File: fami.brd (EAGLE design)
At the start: 86.4 x 50.8 mm, 14 parts, among them IC1 PROM, IC2 WRAM, IC3 CHROM, IC4 74LS20N

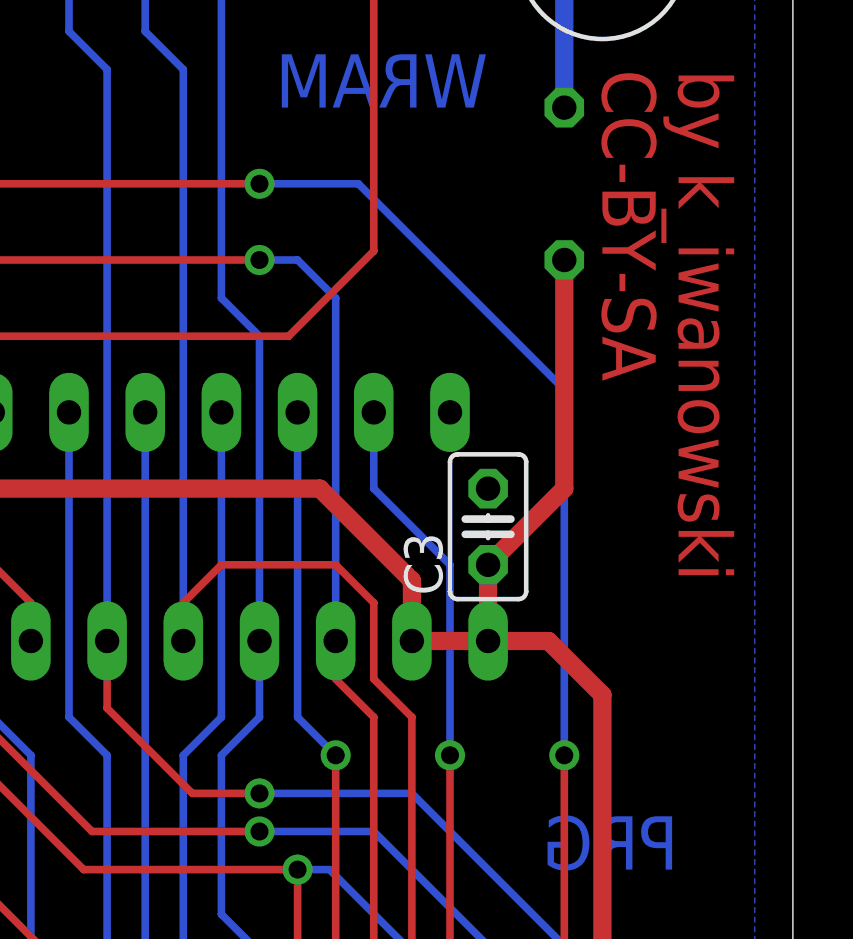
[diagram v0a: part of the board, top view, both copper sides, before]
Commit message: Added R and C values
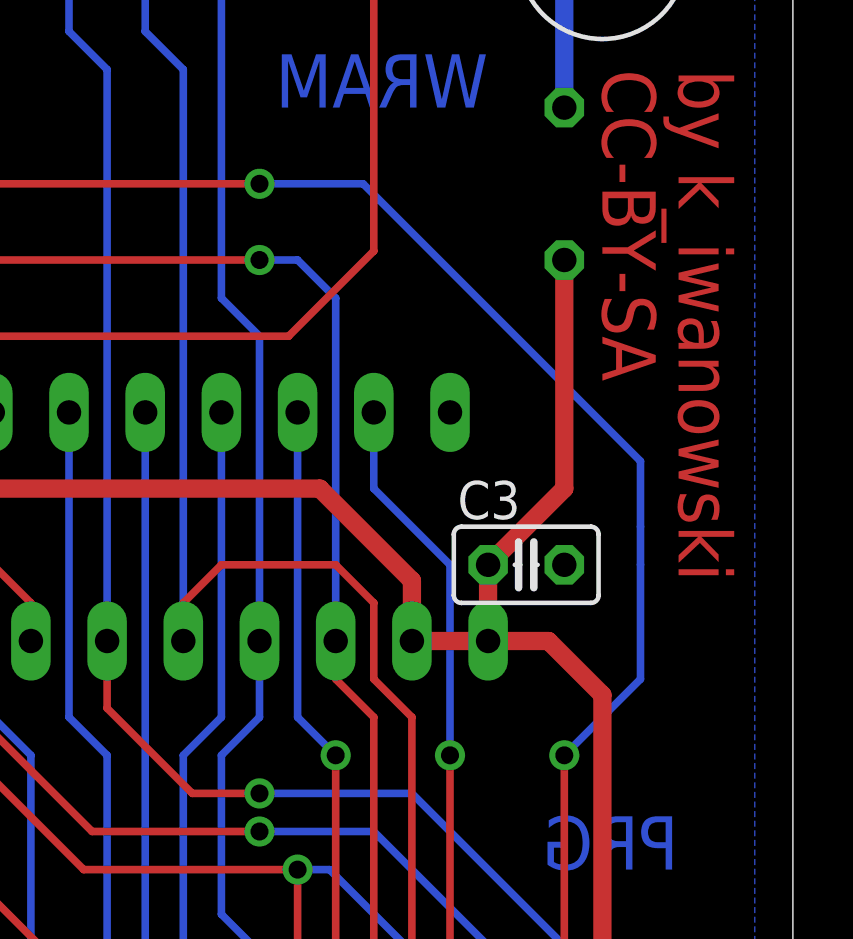
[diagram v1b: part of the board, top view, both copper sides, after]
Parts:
- C1: value (none) -> 10u
- C2, C3: value (none) -> 100n
- R1, R2: value (none) -> 1k
- moved C3 1.80 mm to (76.2, 22.9), turned to 0 degrees
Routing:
- net O2: track 88.9 -> 91.1 mm
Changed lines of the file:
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@@
 <element name="D2" library="diode" package="D-5" value="" x="35.56" y="48.26" rot="MR0"/>
 <element name="JP1" library="SparkFun-Connectors" package="1X03" value="" x="26.67" y="25.4" rot="MR0"/>
-<element name="C1" library="rcl" package="E2,5-6" value="" x="78.74" y="43.18"/>
-<element name="C2" library="rcl" package="C025-025X050" value="" x="33.02" y="25.4" rot="R180"/>
-<element name="R1" library="rcl" package="0204/7" value="" x="44.45" y="48.26" rot="R180"/>
-<element name="R2" library="rcl" package="0204/7" value="" x="44.45" y="45.72"/>
-<element name="C3" library="rcl" package="C025-025X050" value="" x="74.93" y="24.13" rot="R90"/>
+<element name="C1" library="rcl" package="E2,5-6" value="10u" x="78.74" y="43.18"/>
+<element name="C2" library="rcl" package="C025-025X050" value="100n" x="33.02" y="25.4" rot="R180"/>
+<element name="R1" library="rcl" package="0204/7" value="1k" x="44.45" y="48.26" rot="R180"/>
+<element name="R2" library="rcl" package="0204/7" value="1k" x="44.45" y="45.72"/>
+<element name="C3" library="rcl" package="C025-025X050" value="100n" x="76.2" y="22.86"/>
 <element name="G2" library="battery" package="B2430UNI" value="B2430UNI" x="11.43" y="38.1" rot="R180"/>
 </elements>
@@
 <wire x1="77.47" y1="2.54" x2="77.47" y2="16.51" width="0.254" layer="1"/>
 <via x="77.47" y="16.51" extent="1-16" drill="0.6"/>
-<wire x1="77.47" y1="16.51" x2="77.47" y2="28.698034375" width="0.254" layer="16"/>
-<wire x1="77.47" y1="28.698034375" x2="70.608034375" y2="35.56" width="0.254" layer="16"/>
-<wire x1="70.608034375" y1="35.56" x2="67.31" y2="35.56" width="0.254" layer="16"/>
+<wire x1="77.47" y1="16.51" x2="80.01" y2="19.05" width="0.254" layer="16"/>
+<wire x1="80.01" y1="19.05" x2="80.01" y2="22.86" width="0.254" layer="16"/>
+<wire x1="80.01" y1="22.86" x2="80.01" y2="24.13" width="0.254" layer="16"/>
 <via x="67.31" y="35.56" extent="1-16" drill="0.6"/>
 <wire x1="67.31" y1="35.56" x2="33.76395" y2="35.56" width="0.254" layer="1"/>
 <wire x1="33.76395" y1="35.56" x2="29.95395" y2="39.37" width="0.254" layer="1"/>
 <wire x1="29.95395" y1="39.37" x2="27.94" y2="39.37" width="0.254" layer="1"/>
+<wire x1="67.31" y1="35.56" x2="70.7642625" y2="35.56" width="0.254" layer="16"/>
+<wire x1="70.7642625" y1="35.56" x2="80.01" y2="26.3142625" width="0.254" layer="16"/>
+<wire x1="80.01" y1="26.3142625" x2="80.01" y2="24.13" width="0.254" layer="16"/>
 </signal>
 <signal name="VRAMA10">

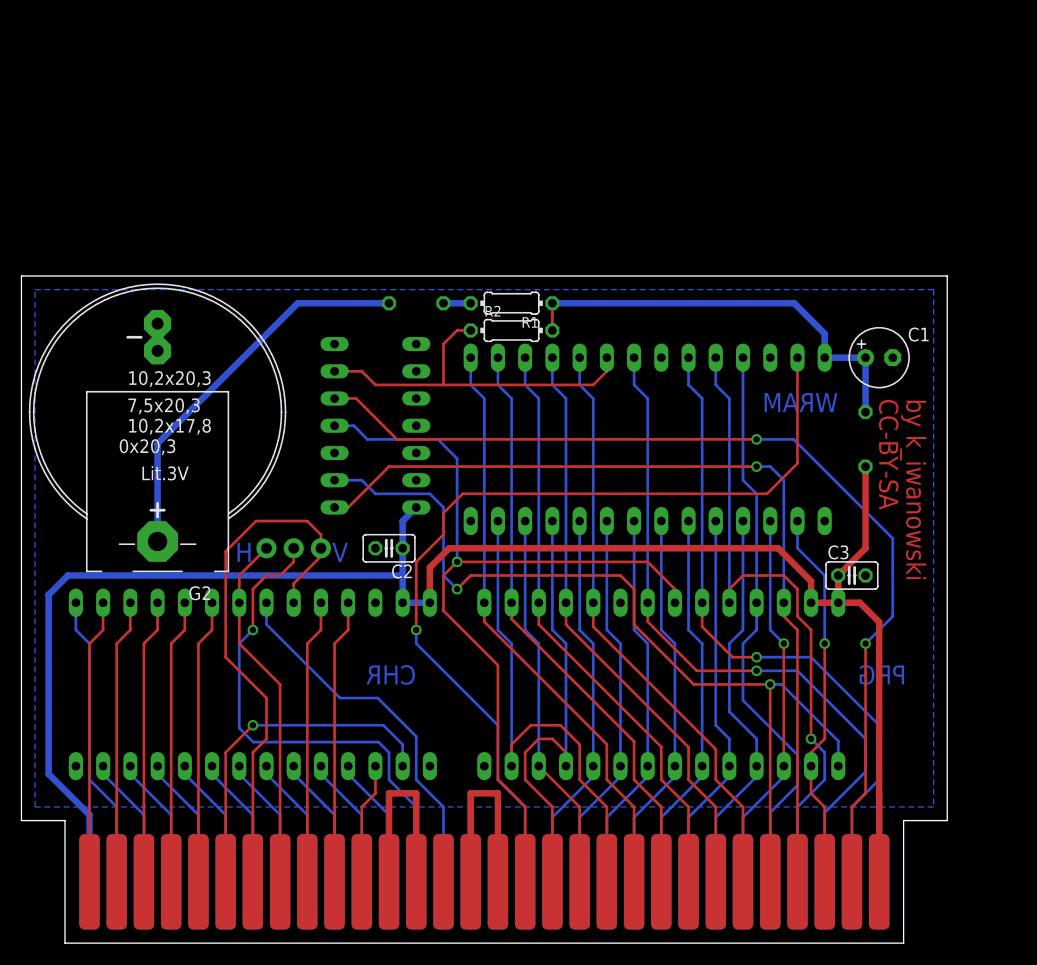
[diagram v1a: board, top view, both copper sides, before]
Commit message: Added support for CNROM and GNROM
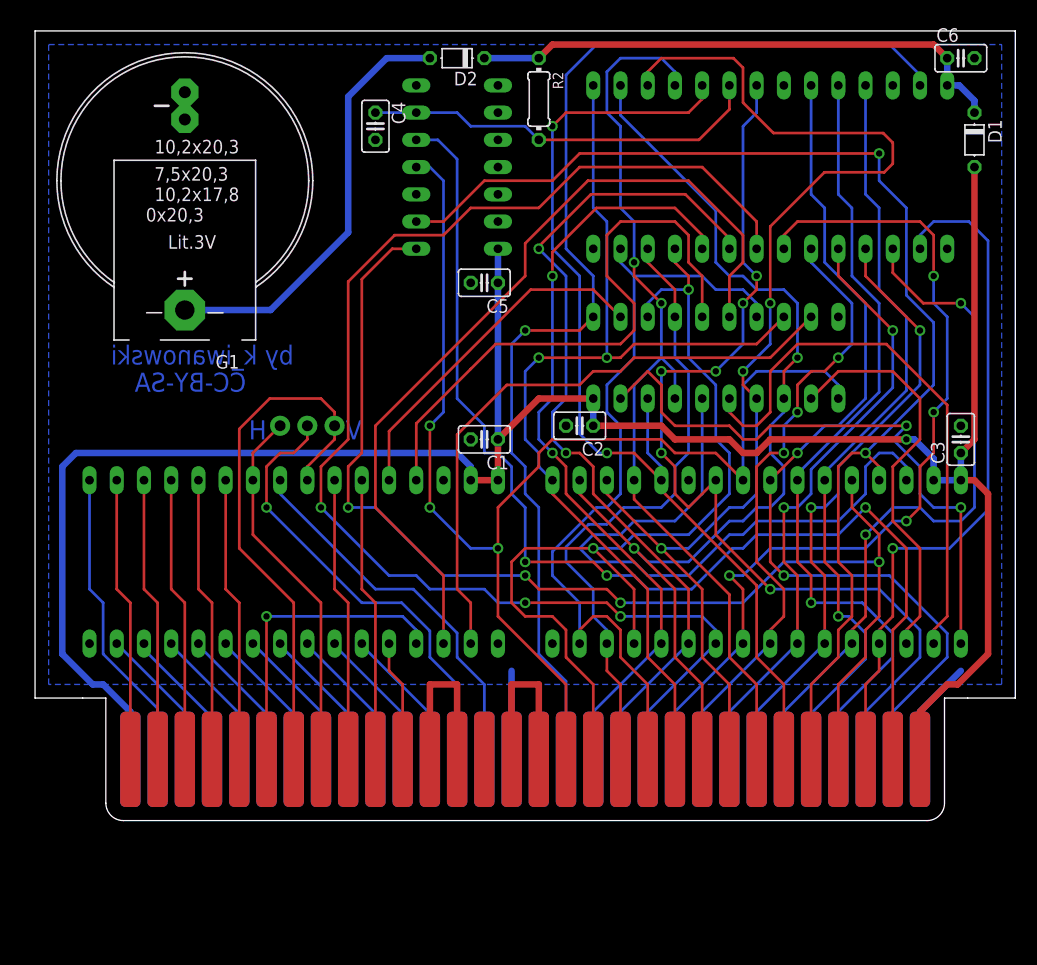
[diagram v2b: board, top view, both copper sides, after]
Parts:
- removed G2: B2430UNI, battery:B2430UNI
- removed R1: 1k, rcl:0204/7
- added C4: 1nF, rcl:C025-025X050
- added C5, C6: 100nF, rcl:C025-025X050
- added G1: B2430UNI, battery:B2430UNI
- added IC5: 74LS20N, 74xx-eu:DIL14
- C1: value 10u -> 100nF; device rcl:E2,5-6 -> rcl:C025-025X050
- C2, C3: value 100n -> 100nF
- IC1: value PROM -> PRGROM; device ic-package:DIL28-6 -> ic-package:DIL32
- IC2: value WRAM -> 74LS377N; device ic-package:DIL28-6 -> 74xx-us:DIL20
- IC3: device ic-package:DIL28-6 -> ic-package:DIL32
- IC4: value 74LS20N -> (none); device 74xx-eu:DIL14 -> ic-package:DIL28-6
- R2: value 1k -> 100k
- moved IC4 44.0 mm to (68.6, 61.0), turned to 0 degrees
- moved C1 37.6 mm to (41.9, 35.6), turned to 180 degrees
- moved D1 29.7 mm to (87.6, 63.5), flipped to the top
- moved D2 23.2 mm to (39.4, 71.1), flipped to the top, turned to 180 degrees
- moved R2 21.7 mm to (47.0, 67.3), turned to 270 degrees
- moved C2 21.1 mm to (50.8, 36.8)
- moved C3 16.3 mm to (86.4, 35.6), turned to 90 degrees
- moved IC1 14.5 mm to (67.3, 24.1)
- moved U$1 12.0 mm to (38.1, 6.35)
- moved IC3 12.0 mm to (24.1, 24.1)
- moved JP1 11.5 mm to (27.9, 36.8)
- moved IC2 9.92 mm to (63.5, 43.2), turned to 180 degrees
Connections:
- removed net N$24: C1.+, D1.C, IC2.28, R1.1, R2.2
- removed net N$4: D2.A, G2.+@4
- new net A15: IC1.3, IC2.12
- new net A16: IC1.2, IC2.15
- new net A17: IC1.30, IC2.16
- new net A18: IC1.1, IC2.19
- new net N$7: C4.1, IC4.20, IC5.6, R2.2
- new net N$9: D2.A, G1.+@4
- new net PA14: IC2.5, IC3.29
- new net PA15: IC2.6, IC3.3
- new net PA16: IC2.9, IC3.2
- net A0: now also IC1.12, IC4.10; no longer IC1.10, IC2.10
- net A1: now also IC1.11, IC4.9; no longer IC1.9, IC2.9
- net A10: now also IC1.23, IC4.21; no longer IC1.21, IC2.21
- net A11: now also IC1.25, IC4.23; no longer IC1.23, IC2.23
- net A12: now also IC1.4, IC4.2; no longer IC1.2, IC2.2
- net A13: now also IC1.28, IC5.1; no longer IC1.26, IC4.1
- net A14: now also IC1.29, IC5.2; no longer IC1.1, IC4.2
- net A2: now also IC1.10, IC4.8; no longer IC1.8, IC2.8
- net A3: now also IC1.9, IC4.7; no longer IC1.7, IC2.7
- net A4: now also IC1.8, IC4.6; no longer IC1.6, IC2.6
- net A5: now also IC1.7, IC4.5; no longer IC1.5, IC2.5
- net A6: now also IC1.6, IC4.4; no longer IC1.4, IC2.4
- net A7: now also IC1.5, IC4.3; no longer IC1.3, IC2.3
- net A8: now also IC1.27, IC4.25; no longer IC1.25, IC2.25
- net A9: now also IC1.26, IC4.24; no longer IC1.24, IC2.24
- net D0: now also IC1.13, IC2.3, IC4.11; no longer IC1.11, IC2.11
- net D1: now also IC1.14, IC2.4, IC4.12; no longer IC1.12, IC2.12
- net D2: now also IC1.15, IC2.7, IC4.13; no longer IC1.13, IC2.13
- net D3: now also IC1.17, IC2.8, IC4.15; no longer IC1.15, IC2.15
- net D4: now also IC1.18, IC2.13, IC4.16; no longer IC1.16, IC2.16
- net D5: now also IC1.19, IC2.14, IC4.17; no longer IC1.17, IC2.17
- net D6: now also IC1.20, IC2.17, IC4.18; no longer IC1.18, IC2.18
- net D7: now also IC1.21, IC2.18, IC4.19; no longer IC1.19, IC2.19
- net GND: now also C1.2, C4.2, C5.2, C6.2, G1.-, G1.-@1, IC1.16, IC1.22, IC2.10, IC3.16, IC3.30, IC4.1, IC4.14, IC4.22, IC4.26, IC5.7; no longer C1.-, G2.-, G2.-@1, IC1.14, IC1.20, IC2.1, IC2.14, IC2.22, IC2.26, IC3.14, IC3.26, IC4.7
- net N$1: now also IC2.2, IC3.28; no longer D2.C, R1.2
- net N$6: now also C6.1, D1.C, D2.C, IC4.28; no longer IC2.20, IC4.6
- net O2: now also IC5.5; no longer IC4.5
- net PA0: now also IC3.12; no longer IC3.10
- net PA1: now also IC3.11; no longer IC3.9
- net PA10: now also IC3.23; no longer IC3.21
- net PA11: now also IC3.25; no longer IC3.23
- net PA12: now also IC3.4; no longer IC3.2
- net PA13: now also IC3.22; no longer IC3.20
- net PA2: now also IC3.10; no longer IC3.8
- net PA3: now also IC3.9; no longer IC3.7
- net PA4: now also IC3.8; no longer IC3.6
- net PA5: now also IC3.7; no longer IC3.5
- net PA6: now also IC3.6; no longer IC3.4
- net PA7: now also IC3.5; no longer IC3.3
- net PA8: now also IC3.27; no longer IC3.25
- net PA9: now also IC3.26; no longer IC3.24
- net PD0: now also IC3.13; no longer IC3.11
- net PD1: now also IC3.14; no longer IC3.12
- net PD2: now also IC3.15; no longer IC3.13
- net PD3: now also IC3.17; no longer IC3.15
- net PD4: now also IC3.18; no longer IC3.16
- net PD5: now also IC3.19; no longer IC3.17
- net PD6: now also IC3.20; no longer IC3.18
- net PD7: now also IC3.21; no longer IC3.19
- net RD: now also IC3.24; no longer IC3.22
- net ROMSEL: now also IC1.24, IC2.11, IC5.4; no longer IC1.22, IC4.4
- net RW: now also IC2.1, IC4.27; no longer IC2.27
- net VCC: now also C1.1, C5.1, IC1.31, IC1.32, IC2.20, IC3.31, IC3.32, IC5.14; no longer IC1.27, IC1.28, IC3.27, IC3.28, IC4.14
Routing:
- net A2: track 35.8 -> 125.5 mm, vias 0 -> 3
- net PA15: track 0.00 -> 78.7 mm
- net A17: track 0.00 -> 62.0 mm
- net D5: track 55.2 -> 113.9 mm, vias 0 -> 3
- net PA16: track 0.00 -> 57.6 mm
- net A18: track 0.00 -> 57.3 mm, vias 0 -> 2
- net PA14: track 0.00 -> 56.0 mm
- net A16: track 0.00 -> 52.6 mm
- net A3: track 35.8 -> 84.0 mm, vias 0 -> 4
- net VCC: track 162.0 -> 207.5 mm, vias 0 -> 1
- net A1: track 35.8 -> 80.5 mm, vias 0 -> 2
- net D0: track 42.6 -> 87.0 mm, vias 0 -> 2
- net D4: track 55.2 -> 96.6 mm, vias 0 -> 2
- net N$24: track 40.2 -> 0.00 mm
- net N$9: track 0.00 -> 40.0 mm
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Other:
- board size 86.4 x 50.8 mm -> 91.4 x 62.2 mm
- board text removed: "CHR"
- board text removed: "PRG"
- board text removed: "WRAM"
